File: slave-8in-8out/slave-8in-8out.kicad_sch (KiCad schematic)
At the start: 38 parts, among them J1 Conn_01x06_Male, J2 Screw_Terminal_01x02, J3 Conn_01x06_Female, J4 Screw_Terminal_01x04, J5 Screw_Terminal_01x04, J6 Screw_Terminal_01x04, J7 Screw_Terminal_01x04, J8 Conn_01x10_Male, J9 Screw_Terminal_01x02, SW1 SW_DIP_x05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

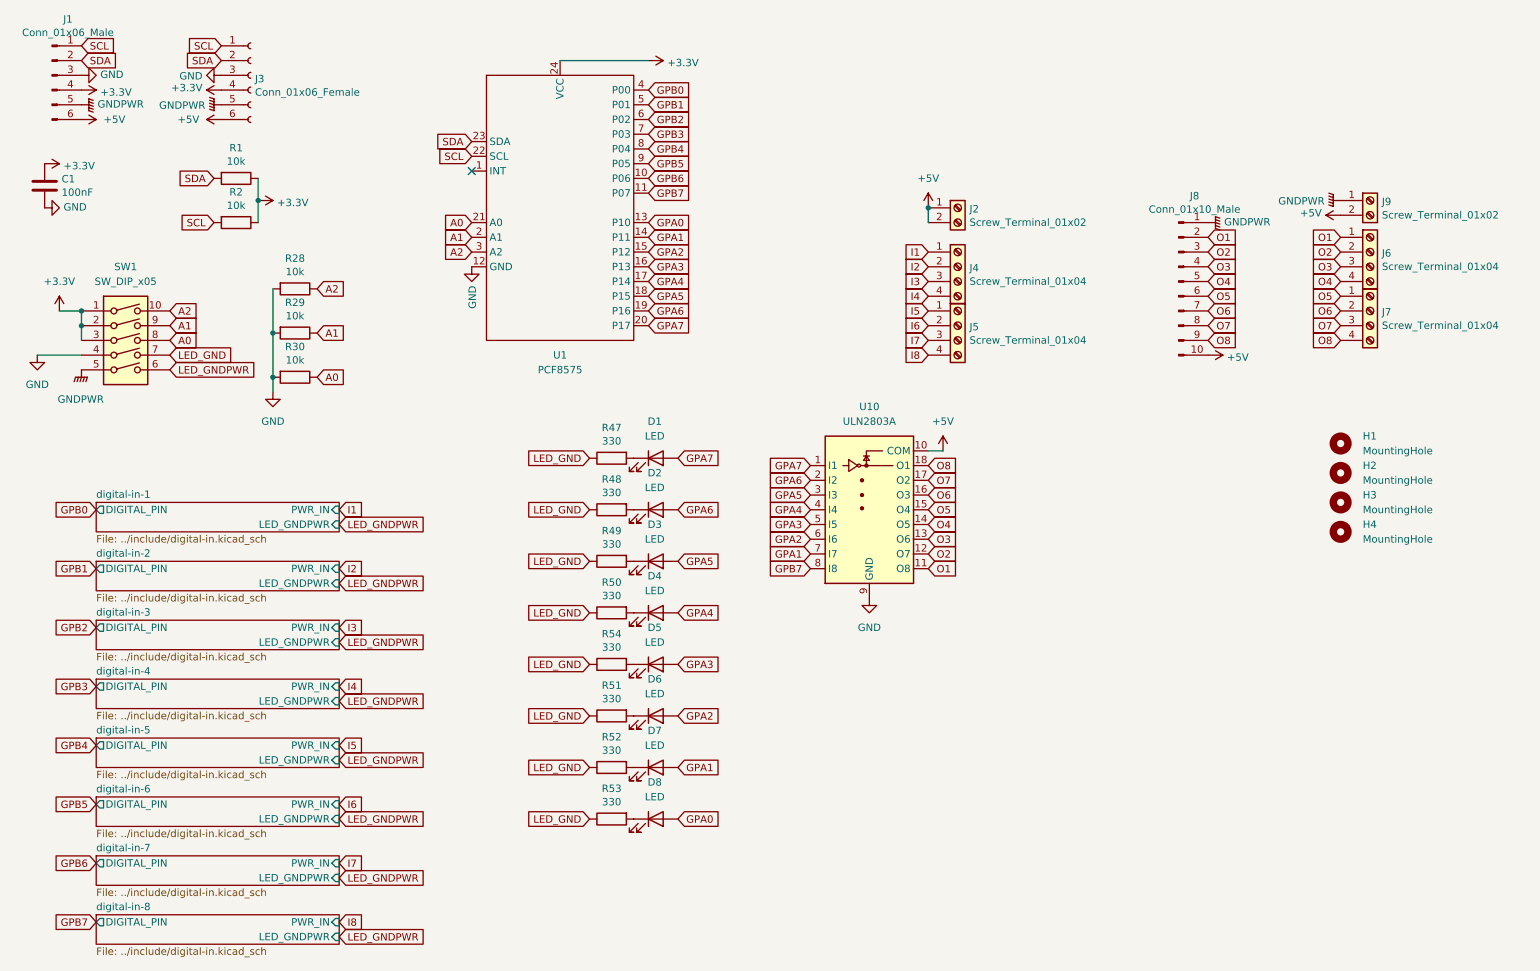
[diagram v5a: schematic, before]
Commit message: refactoring slave-8in-8out
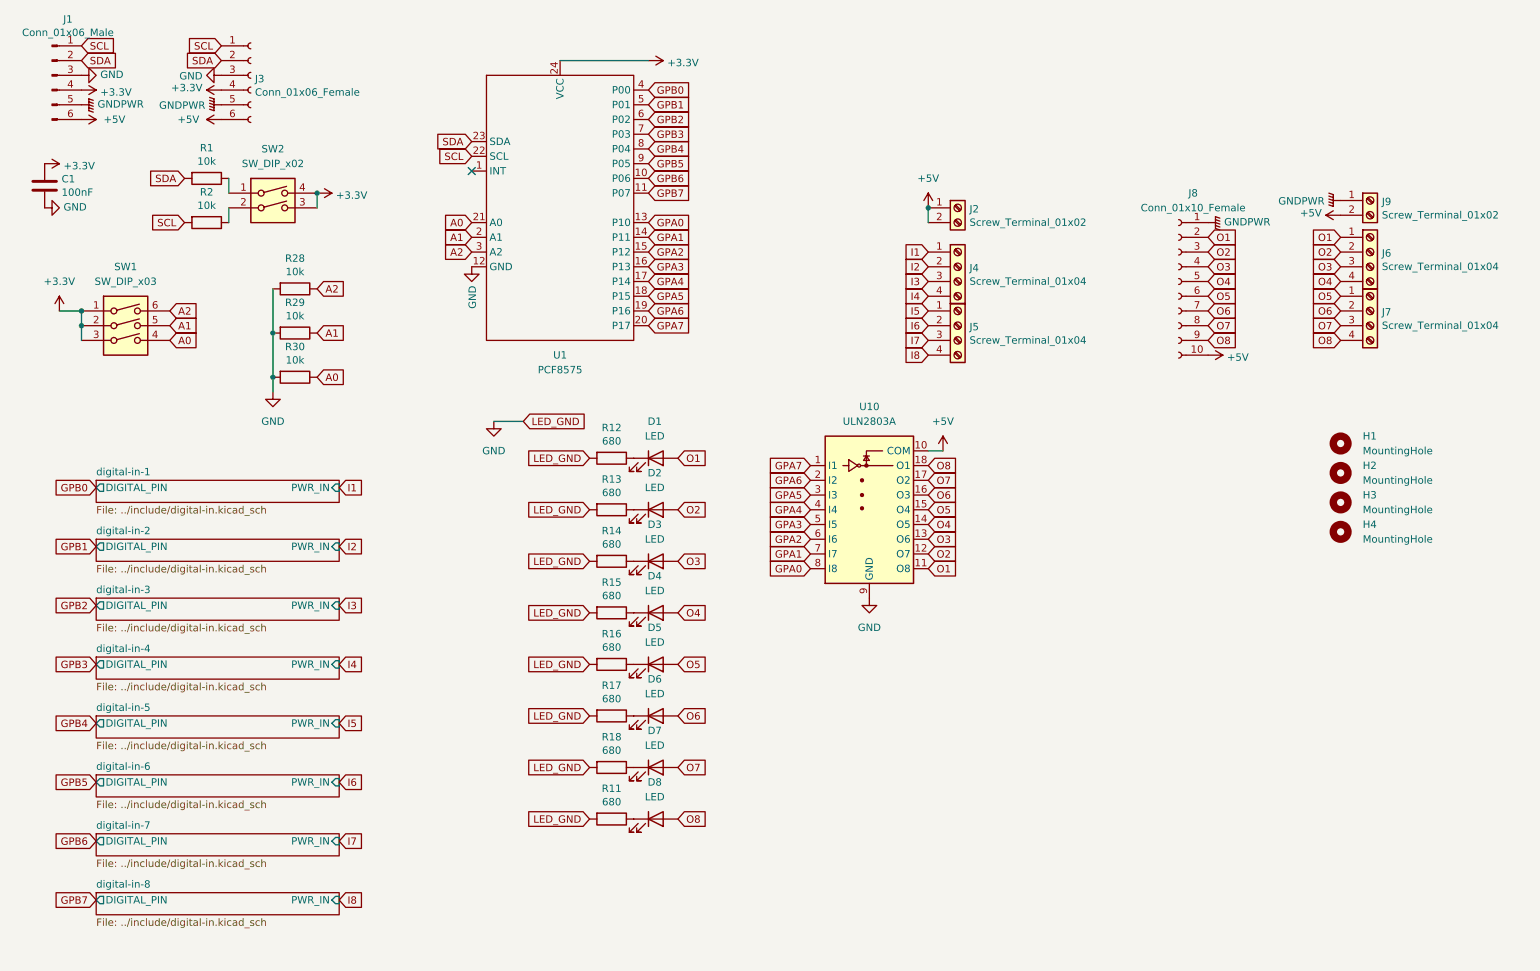
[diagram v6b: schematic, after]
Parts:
- removed J8: Conn_01x10_Male, Connector_PinHeader_2.54mm:PinHeader_1x10_P2.54mm_Vertical, symbol Connector:Conn_01x10_Male
- removed R47, R48, R49, R50, R51, R52, R53, R54: 330, Resistor_SMD:R_0402_1005Metric, symbol Device:R
- removed SW1: SW_DIP_x05, Button_Switch_THT:SW_DIP_SPSTx05_Slide_9.78x14.88mm_W7.62mm_P2.54mm, symbol Switch:SW_DIP_x05
- added J8: Conn_01x10_Female, Connector_PinSocket_2.54mm:PinSocket_1x10_P2.54mm_Vertical, symbol Connector:Conn_01x10_Female
- added R11, R12, R13, R14, R15, R16, R17, R18: 680, Resistor_SMD:R_0402_1005Metric, symbol Device:R
- added SW1: SW_DIP_x03, Button_Switch_THT:SW_DIP_SPSTx03_Slide_9.78x9.8mm_W7.62mm_P2.54mm, symbol Switch:SW_DIP_x03
- added SW2: SW_DIP_x02, Button_Switch_THT:SW_DIP_SPSTx02_Slide_9.78x7.26mm_W7.62mm_P2.54mm, symbol Switch:SW_DIP_x02
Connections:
- net +3V3: now also SW1.1, SW1.2, SW1.3, SW2.3, SW2.4; no longer R1.1, R2.1
- net +5V: now also J8.10 (Pin_10)
- net A0: now also SW1.4
- net A1: now also SW1.5
- net A2: now also SW1.6
- net GND: now also R11.2, R12.2, R13.2, R14.2, R15.2, R16.2, R17.2, R18.2
- net GNDPWR: now also J8.1 (Pin_1)
- net GPA0: now also U10.8 (I8); no longer D8.2 (A)
- net GPA1: no longer D7.2 (A)
- net GPA2: no longer D6.2 (A)
- net GPA3: no longer D5.2 (A)
- net GPA4: no longer D4.2 (A)
- net GPA5: no longer D3.2 (A)
- net GPA6: no longer D2.2 (A)
- net GPA7: no longer D1.2 (A)
- net GPB7: no longer U10.8 (I8)
- net O1: now also D1.2 (A), J8.2 (Pin_2)
- net O2: now also D2.2 (A), J8.3 (Pin_3)
- net O3: now also D3.2 (A), J8.4 (Pin_4)
- net O4: now also D4.2 (A), J8.5 (Pin_5)
- net O5: now also D5.2 (A), J8.6 (Pin_6)
- net O6: now also D6.2 (A), J8.7 (Pin_7)
- net O7: now also D7.2 (A), J8.8 (Pin_8)
- net O8: now also D8.2 (A), J8.9 (Pin_9)
- net at D3.1 (K): now also R14.1
- net at D1.1 (K): now also R12.1
- net at D8.1 (K): now also R11.1
- net at D2.1 (K): now also R13.1
- net at D6.1 (K): now also R17.1
- net at D5.1 (K): now also R16.1
- net at D4.1 (K): now also R15.1
- net at D7.1 (K): now also R18.1
- new net: R1.1, SW2.1
- new net: R2.1, SW2.2
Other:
- sheet digital-in-1 ports: added none; removed LED_GNDPWR
- sheet digital-in-2 ports: added none; removed LED_GNDPWR
- sheet digital-in-3 ports: added none; removed LED_GNDPWR
- sheet digital-in-4 ports: added none; removed LED_GNDPWR
- sheet digital-in-5 ports: added none; removed LED_GNDPWR
- sheet digital-in-6 ports: added none; removed LED_GNDPWR
- sheet digital-in-7 ports: added none; removed LED_GNDPWR
- sheet digital-in-8 ports: added none; removed LED_GNDPWR
- moved on the sheet: R1, R2

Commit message: update slave-8in-8out
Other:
- added sheet pcf8575 (pcf8575.kicad_sch)
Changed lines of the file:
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@@
+    )
+  )
+  (sheet (at 201.93 133.35) (size 19.05 5.08) (fields_autoplaced)
+    (stroke (width 0.1524) (type solid) (color 0 0 0 0))
+    (fill (color 0 0 0 0.0000))
+    (property "Sheet name" "pcf8575" (id 0) (at 201.93 132.6384 0)
+      (effects (font (size 1.27 1.27)) (justify left bottom))
+    )
+    (property "Sheet file" "pcf8575.kicad_sch" (id 1) (at 201.93 139.0146 0)
+      (effects (font (size 1.27 1.27)) (justify left top))
     )
   )
@@
     (path "/00000000-0000-0000-0000-0000601f5881" (page "8"))
     (path "/00000000-0000-0000-0000-0000601f5cf2" (page "9"))
+    (path "/fa0a5900-a1ef-4e92-bcad-cb1c90b300b1" (page "10"))
   )
   (symbol_instances
@@
       (reference "#PWR0141") (unit 1) (value "GND") (footprint "")
     )
+    (path "/fa0a5900-a1ef-4e92-bcad-cb1c90b300b1/38006c44-84e9-42c7-85bd-0e4f5e5d2db7"
+      (reference "#PWR?") (unit 1) (value "+5V") (footprint "")
+    )
+    (path "/fa0a5900-a1ef-4e92-bcad-cb1c90b300b1/505b2401-a598-42b8-9445-328ae8659a90"
+      (reference "#PWR?") (unit 1) (value "GND") (footprint "")
+    )
+    (path "/fa0a5900-a1ef-4e92-bcad-cb1c90b300b1/83ffefde-ce05-4556-8bd6-1d62997ab87f"
+      (reference "#PWR?") (unit 1) (value "+3.3V") (footprint "")
+    )
+    (path "/fa0a5900-a1ef-4e92-bcad-cb1c90b300b1/85196acd-4529-4db2-9c5d-44ba5e393679"
+      (reference "#PWR?") (unit 1) (value "GND") (footprint "")
+    )
+    (path "/fa0a5900-a1ef-4e92-bcad-cb1c90b300b1/cd862215-ec9f-46f2-b36f-aa981bf12bad"
+      (reference "#PWR?") (unit 1) (value "+3.3V") (footprint "")
+    )
     (path "/00000000-0000-0000-0000-000060167899"
       (reference "C1") (unit 1) (value "100nF") (footprint "Capacitor_SMD:C_0805_2012Metric")
@@
       (reference "D23") (unit 1) (value "LED") (footprint "Resistor_SMD:R_0805_2012Metric")
     )
+    (path "/fa0a5900-a1ef-4e92-bcad-cb1c90b300b1/c5790c71-4083-48bd-b512-02fb0b855ba1"
+      (reference "D?") (unit 1) (value "LED") (footprint "")
+    )
     (path "/eee10ae1-7e56-41a5-a4ef-cb8260ee8633"
       (reference "H1") (unit 1) (value "MountingHole") (footprint "MountingHole:MountingHole_3.2mm_M3")
@@
       (reference "R46") (unit 1) (value "10k") (footprint "Resistor_SMD:R_0402_1005Metric")
     )
+    (path "/fa0a5900-a1ef-4e92-bcad-cb1c90b300b1/114d526e-7b90-4a3d-931c-832a99d0b7ee"
+      (reference "R?") (unit 1) (value "330") (footprint "")
+    )
     (path "/83371df5-ff86-4aed-8833-f8e97a1f35d5"
       (reference "SW1") (unit 1) (value "SW_DIP_x03") (footprint "Button_Switch_THT:SW_DIP_SPSTx03_Slide_9.78x9.8mm_W7.62mm_P2.54mm")
@@
       (reference "U10") (unit 1) (value "ULN2803A") (footprint "Package_SO:SOIC-18W_7.5x11.6mm_P1.27mm")
     )
+    (path "/fa0a5900-a1ef-4e92-bcad-cb1c90b300b1/c36af448-c885-4f13-9bbe-be029e4e9748"
+      (reference "U?") (unit 1) (value "PCF8575") (footprint "Package_SO:SSOP-24_5.3x8.2mm_P0.65mm")
+    )
+    (path "/fa0a5900-a1ef-4e92-bcad-cb1c90b300b1/ee78459a-03b4-495c-860d-0d4ecc5e58ac"
+      (reference "U?") (unit 1) (value "ULN2803A") (footprint "")
+    )
   )

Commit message: update slave-8in-8out
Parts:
- added R19, R20, R21, R22, R23, R24, R25, R26: 10k, Resistor_SMD:R_0402_1005Metric, symbol Device:R
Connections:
- net I8 is gone; now on net I7: J5.4 (Pin_4)
- net +3V3: now also R19.1, R20.1, R21.1, R22.1, R23.1, R24.1, R25.1, R26.1
- net +5V: now also R11.2, R12.2, R13.2, R14.2, R15.2, R16.2, R17.2, R18.2
- net GND: no longer R11.2, R12.2, R13.2, R14.2, R15.2, R16.2, R17.2, R18.2
- net GPA0: now also R26.2
- net GPA1: now also R25.2
- net GPA2: now also R24.2
- net GPA3: now also R23.2
- net GPA4: now also R22.2
- net GPA5: now also R21.2
- net GPA6: now also R20.2
- net GPA7: now also R19.2
- net I1: now also J4.2 (Pin_2); no longer J4.1 (Pin_1)
- net I2: now also J4.3 (Pin_3); no longer J4.2 (Pin_2)
- net I3: now also J4.4 (Pin_4); no longer J4.3 (Pin_3)
- net I4: now also J5.1 (Pin_1); no longer J4.4 (Pin_4)
- net I5: now also J5.2 (Pin_2); no longer J5.1 (Pin_1)
- net I6: now also J5.3 (Pin_3); no longer J5.2 (Pin_2)
- net I7: no longer J5.3 (Pin_3)
- net O1: now also D2.1 (K), J6.2 (Pin_2), J8.3 (Pin_3), U10.12 (O7); no longer D1.2 (A), J6.1 (Pin_1), J8.2 (Pin_2), U10.11 (O8)
- net O2: now also D3.1 (K), J6.3 (Pin_3), J8.4 (Pin_4), U10.13 (O6); no longer D2.2 (A), J6.2 (Pin_2), J8.3 (Pin_3), U10.12 (O7)
- net O3: now also D4.1 (K), J6.4 (Pin_4), J8.5 (Pin_5), U10.14 (O5); no longer D3.2 (A), J6.3 (Pin_3), J8.4 (Pin_4), U10.13 (O6)
- net O4: now also D5.1 (K), J7.1 (Pin_1), J8.6 (Pin_6), U10.15 (O4); no longer D4.2 (A), J6.4 (Pin_4), J8.5 (Pin_5), U10.14 (O5)
- net O5: now also D6.1 (K), J7.2 (Pin_2), J8.7 (Pin_7), U10.16 (O3); no longer D5.2 (A), J7.1 (Pin_1), J8.6 (Pin_6), U10.15 (O4)
- net O6: now also D7.1 (K), J7.3 (Pin_3), J8.8 (Pin_8), U10.17 (O2); no longer D6.2 (A), J7.2 (Pin_2), J8.7 (Pin_7), U10.16 (O3)
- net O7: now also D8.1 (K), J7.4 (Pin_4), J8.9 (Pin_9), U10.18 (O1); no longer D7.2 (A), J7.3 (Pin_3), J8.8 (Pin_8), U10.17 (O2)
- net at R14.1: now also D3.2 (A); no longer D3.1 (K)
- net at R12.1: now also D1.2 (A); no longer D1.1 (K)
- net at R11.1: now also D8.2 (A); no longer D8.1 (K)
- net at R17.1: now also D6.2 (A); no longer D6.1 (K)
- net at R16.1: now also D5.2 (A); no longer D5.1 (K)
- net at R13.1: now also D2.2 (A); no longer D2.1 (K)
- net at R15.1: now also D4.2 (A); no longer D4.1 (K)
- net at R18.1: now also D7.2 (A); no longer D7.1 (K)
- removed net O8: D8.2 (A), J7.4 (Pin_4), J8.9 (Pin_9), U10.18 (O1)
- new net I0: J4.1 (Pin_1)
- new net O0: D1.1 (K), J6.1 (Pin_1), J8.2 (Pin_2), U10.11 (O8)
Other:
- removed sheet digital-in-8
- removed sheet pcf8575
- added sheet digital-in-0 (../include/digital-in.kicad_sch)
- moved on the sheet: D1, D2, D3, D4, D5, D6, D7, D8
